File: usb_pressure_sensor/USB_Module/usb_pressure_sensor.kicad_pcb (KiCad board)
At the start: 2 copper layers, 18 parts, among them IC1 STM32F042F6P6, IC2 MCP1700, J1 CONN_02x09, J2 MODULE_BRIDGE, P1 SWD_TC, SW1 SWITCH_SPST, U1 MICRO_USB, U2 SN74LVC1GX04, Y1 Crystal 32.768kHz

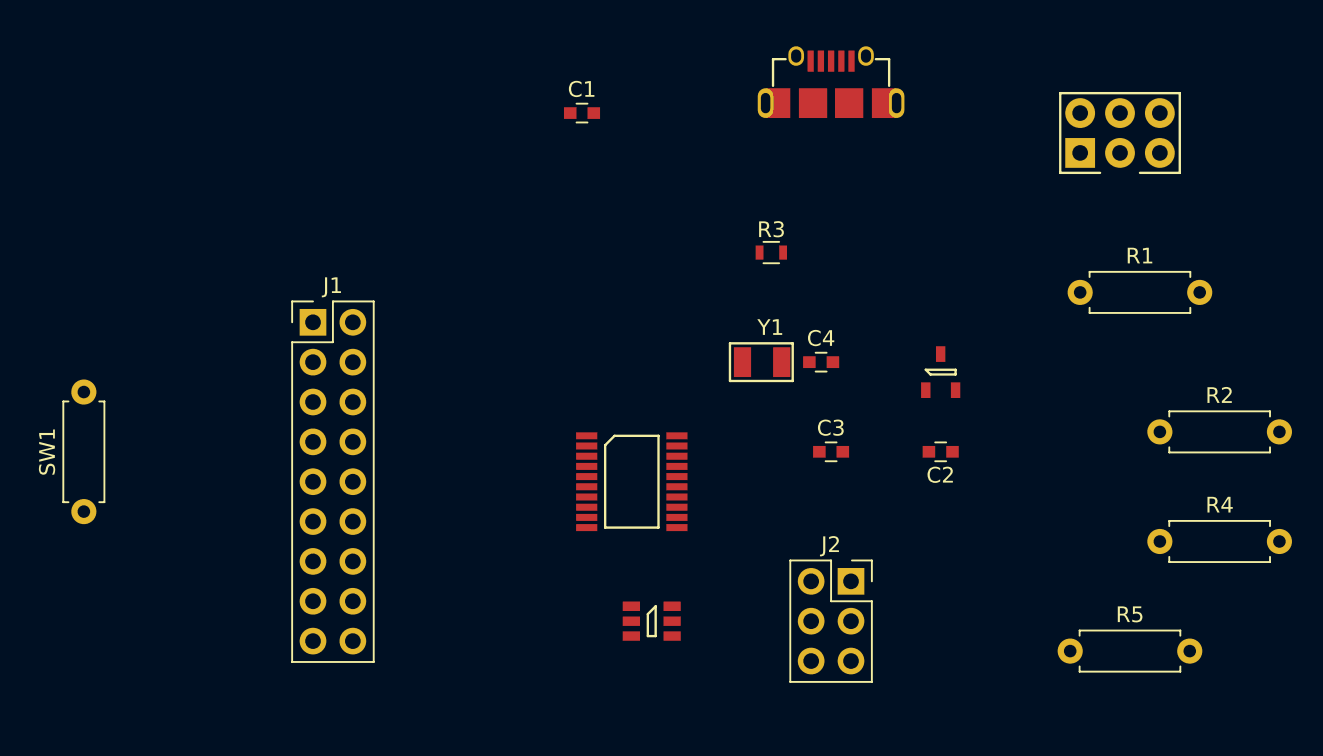
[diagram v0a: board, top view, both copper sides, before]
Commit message: Routed pin header and swd connector
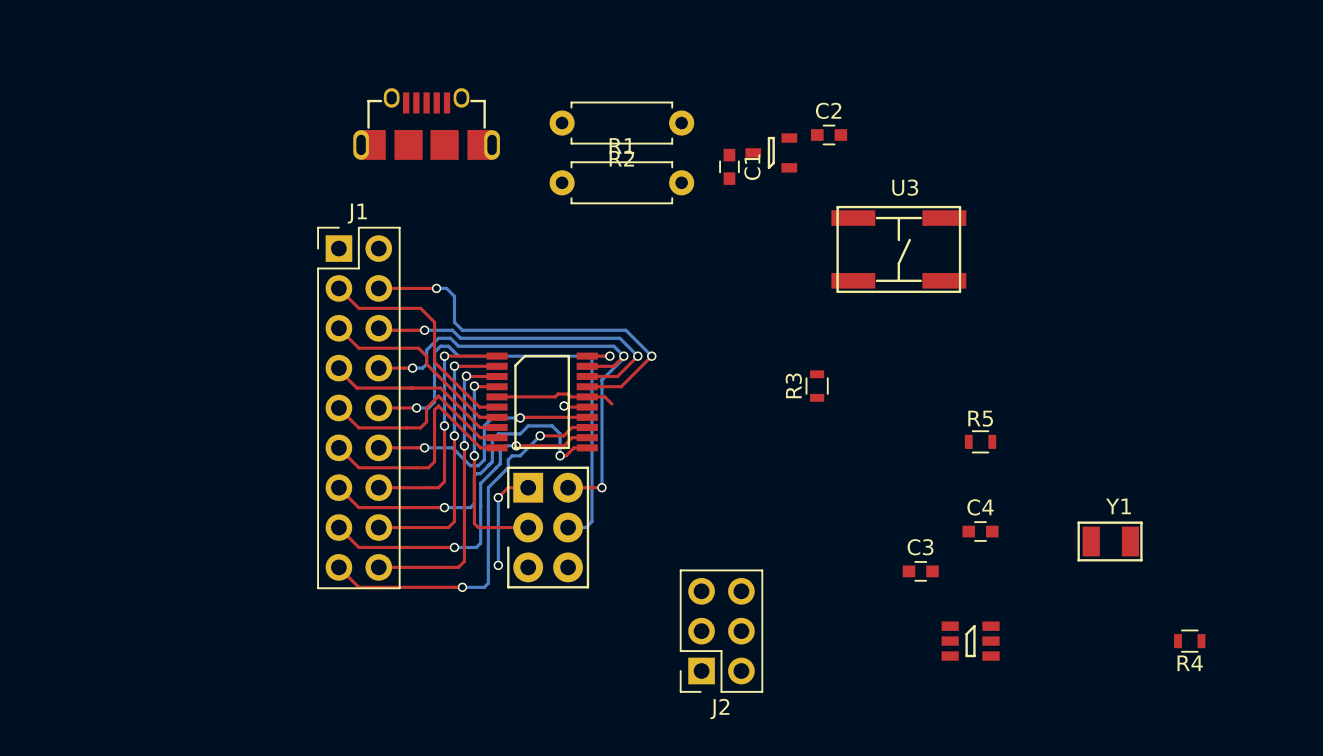
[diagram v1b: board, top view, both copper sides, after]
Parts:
- removed SW1: SWITCH_SPST, Resistors_THT:R_Axial_DIN0207_L6.3mm_D2.5mm_P7.62mm_Horizontal
- added U3: KSC341J:SWITCH, footprints:KSC431J_SWITCH, F.Cu at (156.1, 99.7)
- R4, R5: footprint Resistors_THT:R_Axial_DIN0207_L6.3mm_D2.5mm_P7.62mm_Horizontal -> Resistors_SMD:R_0603
- moved P1 44.3 mm to (133.7, 117.2), turned to 270 degrees
- moved R2 36.3 mm to (142.2, 91.4), turned to 180 degrees
- moved R1 33.8 mm to (134.6, 95.2)
- moved U1 25.9 mm to (126.0, 92.8)
- moved Y1 25.0 mm to (169.5, 118.1)
- moved C2 21.4 mm to (151.6, 92.2), turned to 0 degrees
- moved U2 20.4 mm to (160.7, 124.5)
- moved IC2 17.7 mm to (148.0, 93.3), turned to 180 degrees
- moved C4 14.8 mm to (161.3, 117.5)
- moved R5 14.5 mm to (161.3, 111.8)
- moved J2 11.1 mm to (143.5, 126.4), turned to 180 degrees
- moved C1 10.0 mm to (145.3, 94.2), turned to 270 degrees
- moved C3 9.53 mm to (157.5, 120.0)
- moved R3 9.00 mm to (150.9, 108.2), turned to 90 degrees
- moved IC1 7.65 mm to (133.3, 109.2)
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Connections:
- U2 pad 2: (no net) -> /GND
- U2 pad 3: (no net) -> Net-(C3-Pad1)
- U2 pad 4: (no net) -> /MCLK
- U2 pad 5: (no net) -> /3v3
- U2 pad 6: (no net) -> Net-(U2-Pad6)
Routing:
- net /SWDCLK: track 0.00 -> 32.0 mm, vias 0 -> 2
- net /SWDIO: track 0.00 -> 31.3 mm, vias 0 -> 3
- net /USB_DM: track 0.00 -> 25.1 mm, vias 0 -> 2
- net /DIN: track 0.00 -> 24.8 mm, vias 0 -> 2
- net /SCLK: track 0.00 -> 22.9 mm, vias 0 -> 2
- net /DOUT: track 0.00 -> 22.0 mm, vias 0 -> 2
- net /USB_DP: track 0.00 -> 21.0 mm, vias 0 -> 2
- net /PF1: track 0.00 -> 19.4 mm, vias 0 -> 2
- net /PF0: track 0.00 -> 17.6 mm, vias 0 -> 2
- net /PB1: track 0.00 -> 16.3 mm, vias 0 -> 2
- net /PB8: track 0.00 -> 15.7 mm, vias 0 -> 2
- net /PA4: track 0.00 -> 15.3 mm
- net /PA0: track 0.00 -> 14.7 mm
- net /3v3: track 0.00 -> 14.1 mm, vias 0 -> 2
- net /NRST: track 0.00 -> 13.8 mm, vias 0 -> 2
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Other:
- net class Default: trace_width 0.25 -> 0.2
- rule pad_to_mask_clearance: 0.2 -> 0

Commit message: Finished usb_module routing
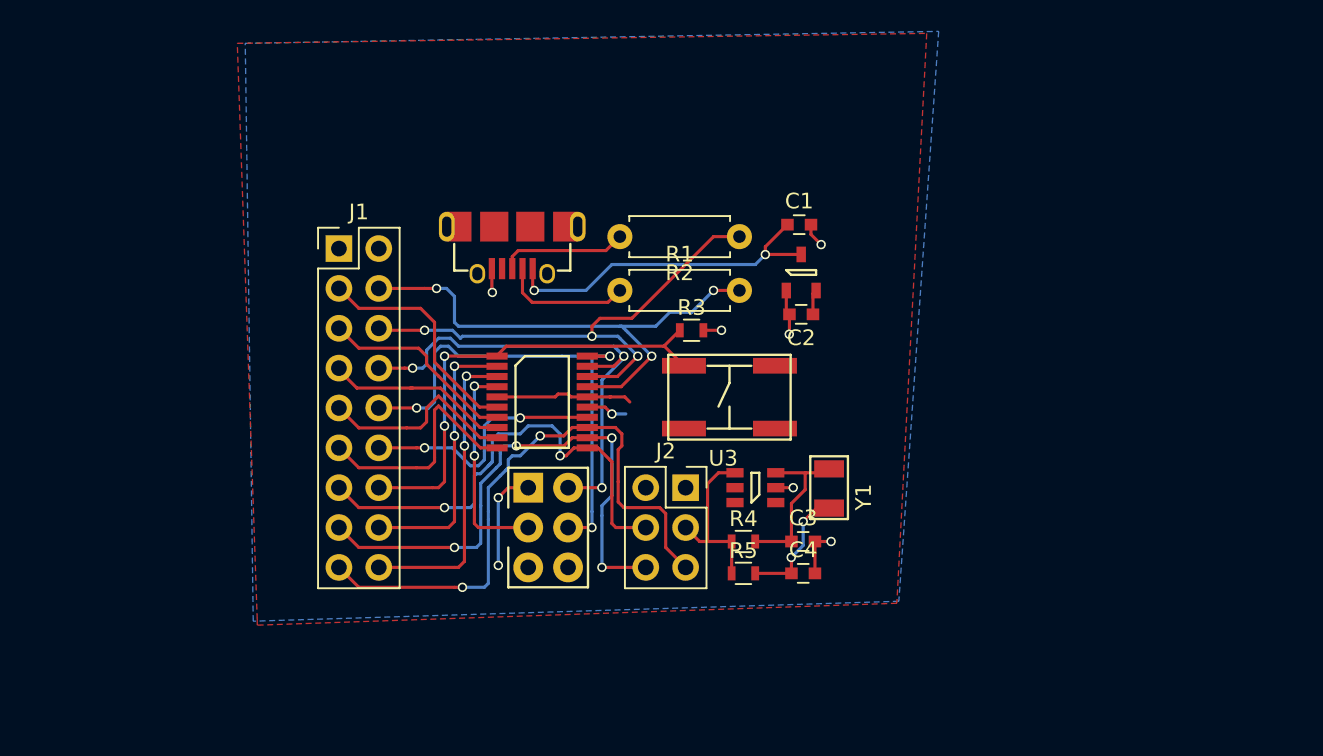
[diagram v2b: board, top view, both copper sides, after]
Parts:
- moved R4 29.1 mm to (146.2, 118.1), turned to 0 degrees
- moved Y1 18.2 mm to (151.6, 114.7), turned to 270 degrees
- moved R5 17.3 mm to (146.2, 120.1)
- moved U2 16.8 mm to (146.9, 114.7), turned to 180 degrees
- moved U3 14.1 mm to (145.3, 108.7), turned to 180 degrees
- moved J2 11.7 mm to (142.5, 114.7), turned to 0 degrees
- moved C4 11.6 mm to (150.0, 120.1)
- moved C2 11.6 mm to (149.9, 103.6), turned to 180 degrees
- moved R3 8.76 mm to (142.9, 104.6), turned to 0 degrees
- moved R2 8.12 mm to (145.9, 98.7)
- moved IC2 7.85 mm to (149.9, 101.0), turned to 90 degrees
- moved R1 7.78 mm to (138.3, 102.1)
- moved C3 7.73 mm to (150.0, 118.1)
- moved U1 7.55 mm to (131.4, 98.0), turned to 180 degrees
- moved C1 5.77 mm to (149.7, 97.9), turned to 0 degrees
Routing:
- net /5v: track 0.00 -> 21.9 mm, vias 0 -> 2
- net /PB8: track 15.7 -> 29.9 mm
- net /DIN: track 24.8 -> 38.9 mm
- net /DOUT: track 22.0 -> 34.9 mm, vias 2 -> 4
- net /USB_DP: track 21.0 -> 33.5 mm, vias 2 -> 3
- net /GND: track 1.51 -> 13.9 mm, vias 1 -> 7
- net /MCLK: track 0.00 -> 11.1 mm
- net Net-(C3-Pad1): track 0.00 -> 10.6 mm
- net /USB_DM: track 25.1 -> 33.6 mm, vias 2 -> 3
- net Net-(R1-Pad1): track 0.00 -> 8.31 mm
- net Net-(R2-Pad2): track 0.00 -> 8.15 mm
- net /SCLK: track 22.9 -> 31.0 mm
- net Net-(C4-Pad1): track 0.00 -> 7.94 mm, vias 0 -> 2
- net /3v3: track 14.1 -> 17.0 mm
- net /SWDCLK: track 32.0 -> 32.4 mm, vias 2 -> 3
- added copper zone on F.Cu, net /3v3
- added copper zone on B.Cu, net /GND

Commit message: added cuts and drills + logos into the PCBs
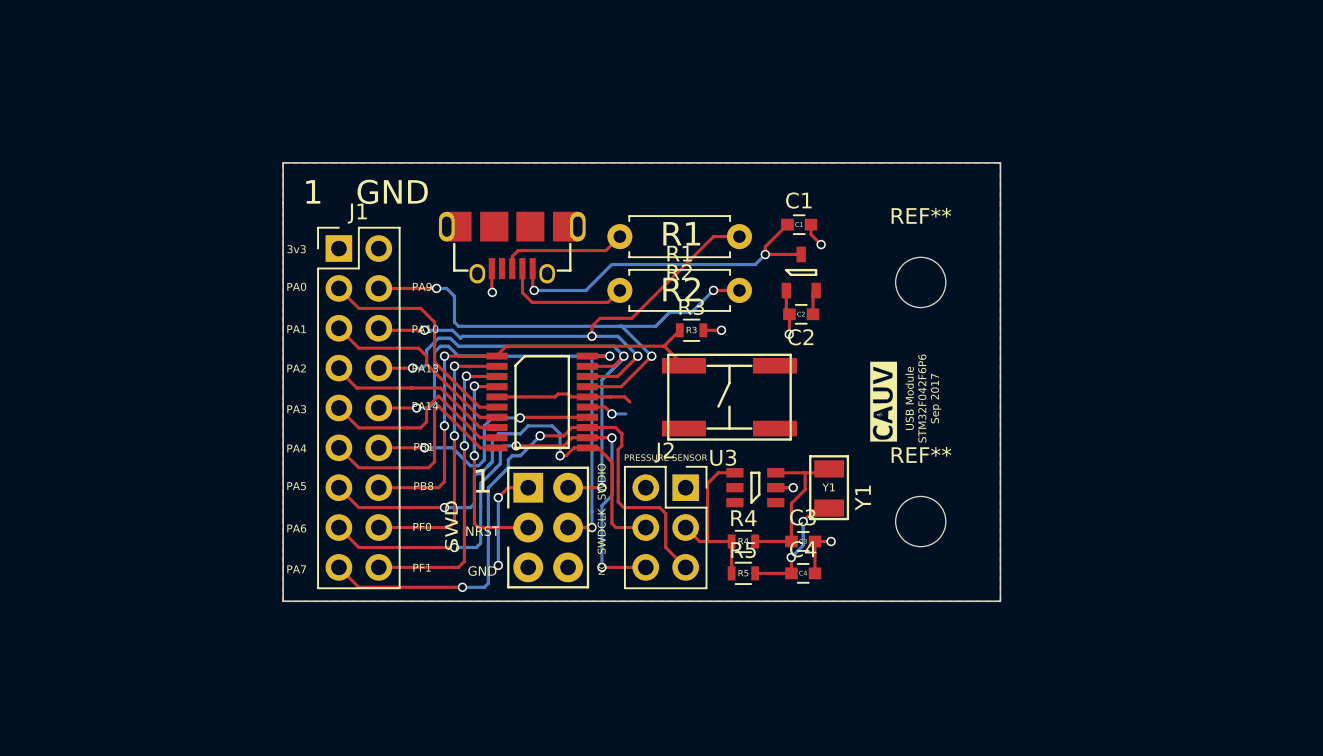
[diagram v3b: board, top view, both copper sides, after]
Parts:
- added G***: LOGO, footprints:LOGO, F.Cu at (155.1, 109.2)
- added REF**: MountingHole_3.2mm_M3, Mounting_Holes:MountingHole_3.2mm_M3, F.Cu at (157.5, 101.6)
- added REF**: MountingHole_3.2mm_M3, Mounting_Holes:MountingHole_3.2mm_M3, F.Cu at (157.5, 116.8)
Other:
- board outline added: 45.7 x 27.9 mm
- board text added: "1"
- board text added: "3v3"
- board text added: "GND"
- board text added: "NC"
- board text added: "NRST"
- board text added: "PA0"
- board text added: "PA1"
- board text added: "PA10"
- board text added: "PA13"
- board text added: "PA14"
- board text added: "PA2"
- board text added: "PA3"
- board text added: "PA4"
- board text added: "PA5"
- board text added: "PA6"
- board text added: "PA7"
- board text added: "PA9"
- board text added: "PB1"
- board text added: "PB8"
- board text added: "PF0"
- board text added: "PF1"
- board text added: "PRESSURE SENSOR"
- board text added: "R1"
- board text added: "R2"
- board text added: "SWD"
- board text added: "SWDCLK"
- board text added: "SWDIO"
- board text added: "USB Module STM32F042F6P6 Sep 2017"
- board text added: "Y1"
